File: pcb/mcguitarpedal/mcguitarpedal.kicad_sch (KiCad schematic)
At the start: 33 parts, among them SW1 LINE_LEVEL, U1 LM4562, U2 Teensy4.1, U3 Teensy4.0_AudioShield_REVD

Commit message: Schematic symbols
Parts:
- removed C1, C3, C4: 470n, symbol ltspice:cap
- removed C2: 570p, symbol ltspice:cap
- removed C5: 10µ, symbol ltspice:cap
- removed C6: 2.2n, symbol ltspice:cap
- removed C7: 4.7n, symbol ltspice:cap
- removed C7: 220n, symbol ltspice:cap
- removed COIL: 2.35, symbol ltspice:ind
- removed R, R10: 10k, symbol Device:R
- removed R1, R5, R6, R7, R8, R9: ${R_BIAS}, symbol Device:R
- removed R11: 4.7k, symbol Device:R
- removed R12: 2.2k, symbol Device:R
- removed R2, R4: ${R_BIAS_IN}, symbol Device:R
- removed R3: 250k, symbol Device:R
- removed R9: 1k, symbol Device:R
- removed RF: 10k, symbol Device:R_Variable
- removed RG: 500, symbol Device:R
- removed SW1: LINE_LEVEL, symbol Switch:SW_Slide_DPDT
- removed U1: LM4562, LM4562:lm4562, symbol Device:Opamp_Dual
- removed VIN: SINE(0 1 3k), symbol ltspice:voltage
- added J1: AudioJack3, Connector_Audio:Jack_6.35mm_Neutrik_NMJ6HFD2-AU_Horizontal, symbol Connector_Audio:AudioJack3
- added J2: Conn_01x05_Pin, Connector_PinHeader_2.54mm:PinHeader_1x05_P2.54mm_Vertical, symbol Connector:Conn_01x04_Pin
- added J3: BTN_MTX, symbol Connector_Generic:Conn_02x08_Row_Letter_Last
- added U4: 74LS148, symbol 74xx:74LS148
- added U5: HEF4094B, symbol 4xxx:HEF4094B
- added U6: LM7805_TO220, Package_TO_SOT_THT:TO-220-3_Vertical, symbol Regulator_Linear:LM7805_TO220
- U2: footprint (none) -> Package_DIP:DIP-48_W15.24mm_Socket_LongPads
- renumbered U3 to U1, V4 to V?, V1 to V?, V2 to V?
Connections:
- net 3.3V: now also U4.16 (VCC)
- net preamp/PREAMP_OUT: now reaches U1.35 (LINE_IN_L)
- net preamp/PREAMP_OUT: now also J2.5 (STAGE2_OUT)
- net at U2.24 (32_OUT1B): now also U4.14 (GS)
- net at U2.38 (16_A2_RX4_SCL1): now also U4.6 (S2)
- net at U2.40 (18_A4_SDA): now also U4.7 (S1)
- net at U2.41 (19_A5_SCL): now also U4.9 (S0)
- new net: J3.5a (Pin_5a), U4.1 (I4)
- new net: J3.1a (Pin_1a), U4.10 (IO)
- new net: J3.2a (Pin_2a), U4.11 (I1)
- new net: J3.3a (Pin_3a), U4.12 (I2)
- new net: J3.4a (Pin_4a), U4.13 (I3)
- new net: J3.6a (Pin_6a), U4.2 (I5)
- new net: J3.7a (Pin_7a), U4.3 (I6)
- new net: J3.8a (Pin_8a), U4.4 (I7)
- new net GND: J1.R, J1.S, J2.1 (GND), J3.1b (Pin_1b), J3.2b (Pin_2b), J3.3b (Pin_3b), J3.4b (Pin_4b), J3.5b (Pin_5b), J3.6b (Pin_6b), J3.7b (Pin_7b), J3.8b (Pin_8b), U4.15 (EO), U4.5 (EI), U4.8 (GND)
- new net preamp/PREAMP_IN: J1.T, J2.2 (PREAMP_IN)
- new net preamp/STAGE1_IN: J2.3 (STAGE1_IN)
- new net preamp/STAGE1_OUT: J2.4 (STAGE1_OUT)
- no-connect marks 0 -> 24
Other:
- added sheet preamp (preamp.kicad_sch)
- note removed: "* .lib LME49710.lib"
- note removed: ".ac dec 100 5 500k .save V(*?*) I(*?*)"
- note removed: ".noise V(PREAMP_OUT) VIN dec 100 2k 1Meg"
- note removed: ".param R=100k"
- note removed: ".param Rbin=1Meg"
- note removed: ".tran 0 15ms 0 100ns"
- note removed: "Instrument"
- note removed: "Line"
- moved on the sheet: U1, U2

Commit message: 4094 wiring
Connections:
- net 3.3V: now also U5.15 (OE), U5.16 (V_{DD})
- net GND: now also U5.8 (V_{SS})
- net at U2.22 (30_CRX3): now also U5.1 (STR)
- net at U2.35 (13_SCK_LED): now also U5.3 (CP)
- net at U2.36 (14_A0_TX3_SPDIF_OUT): now also U5.2 (D)
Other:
- moved on the sheet: J3, U4, U5

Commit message: ILI9488 schematic
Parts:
- removed V?: 5, symbol ltspice:voltage
- removed V?: 9, symbol ltspice:voltage
- added J4: OUT, Connector_Audio:Jack_6.35mm_Neutrik_NMJ6HCD2_Horizontal, symbol Connector_Audio:AudioJack3
- added J5: EXP, Connector_Audio:Jack_6.35mm_Neutrik_NMJ6HCD2_Horizontal, symbol Connector_Audio:AudioJack3
- added J6: ILI9488 Module, Connector_PinHeader_2.54mm:PinHeader_1x14_P2.54mm_Vertical, symbol Connector:Conn_01x14_Pin
- added J7: PWR_IN, symbol Connector:Barrel_Jack
- added U7: STDN-3A24-ADJ, Connector_PinSocket_2.54mm:PinSocket_1x04_P2.54mm_Vertical, symbol Regulator_Linear:LM7805_TO220
- J1: value AudioJack3 -> IN; footprint Connector_Audio:Jack_6.35mm_Neutrik_NMJ6HFD2-AU_Horizontal -> Connector_Audio:Jack_6.35mm_Neutrik_NMJ6HCD2_Horizontal
- J2: value Conn_01x05_Pin -> Conn_01x06_Pin; footprint Connector_PinHeader_2.54mm:PinHeader_1x05_P2.54mm_Vertical -> Connector_PinHeader_2.54mm:PinHeader_1x06_P2.54mm_Vertical
- J3: footprint (none) -> Connector_PinSocket_2.54mm:PinSocket_2x08_P2.54mm_Vertical
- U6: value LM7805_TO220 -> 7805 equivalent SMPS
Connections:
- net 3.3V: now also U1.40 (VOL_3.3V), U7.1 (VO)
- net 5V: now also U2.48 (VIN), U6.3 (VO), J6.1 (VCC), U7.3 (VI), U7.4 (EN)
- net 9V: now also U6.1 (VI), J7.1
- net GND: now also U1.38 (VOL_GND), U2.34 (GND), U2.47 (GND), U6.2 (GND), J6.2 (GND), J7.2, U7.2 (GND)
- net preamp/PREAMP_OUT: now also J2.6 (STAGE2_OUT), U1.34 (LINE_IN_R)
- net at U1.31 (LINE_OUT_L): now also J4.T
- net at U1.32 (LINE_OUT_GND): now also J4.R, J4.S
- net LED_STR: now reaches U2.22 (30_CRX3), U5.1 (STR)
- net 24_BTN_MTX_GS: now reaches U2.24 (32_OUT1B), U4.14 (GS)
- net 33_TFT_CS: now reaches U2.25 (33_MCLK2)
- net 33_TFT_CS: now also J6.3 (CS)
- net 34_TFT_RST: now reaches U2.26 (34_RX8)
- net 34_TFT_RST: now also J6.4 (RESET)
- net 35_TFT_DC/RS: now reaches U2.27 (35_TX8)
- net 35_TFT_DC/RS: now also J6.5 (DC/RS)
- net 36_TOUCH_CS: now reaches U2.28 (36_CS)
- net 36_TOUCH_CS: now also J6.11 (T_CS)
- net 37_TFT_T_IRQ: now reaches U2.29 (37_CS)
- net 37_TFT_T_IRQ: now also J6.14 (T_IRQ)
- net SCK: now reaches U2.35 (13_SCK_LED), U5.3 (CP)
- net LED_DATA: now reaches U2.36 (14_A0_TX3_SPDIF_OUT), U5.2 (D)
- new net 26_TFT_MOSI: J6.12 (T_DIN), J6.6 (SDI(MOSI))
- new net 27_TFT_SCLK: J6.10 (T_CLK), J6.7 (SCK)
- new net 39_TFT_MISO: J6.13 (T_DO), J6.9 (SDO(MISO))
- new net TFT_BACKLIGHT: J6.8 (LED)
- no-connect marks 24 -> 29
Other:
- moved on the sheet: J1, J3, U1, U2, U4, U5, U6

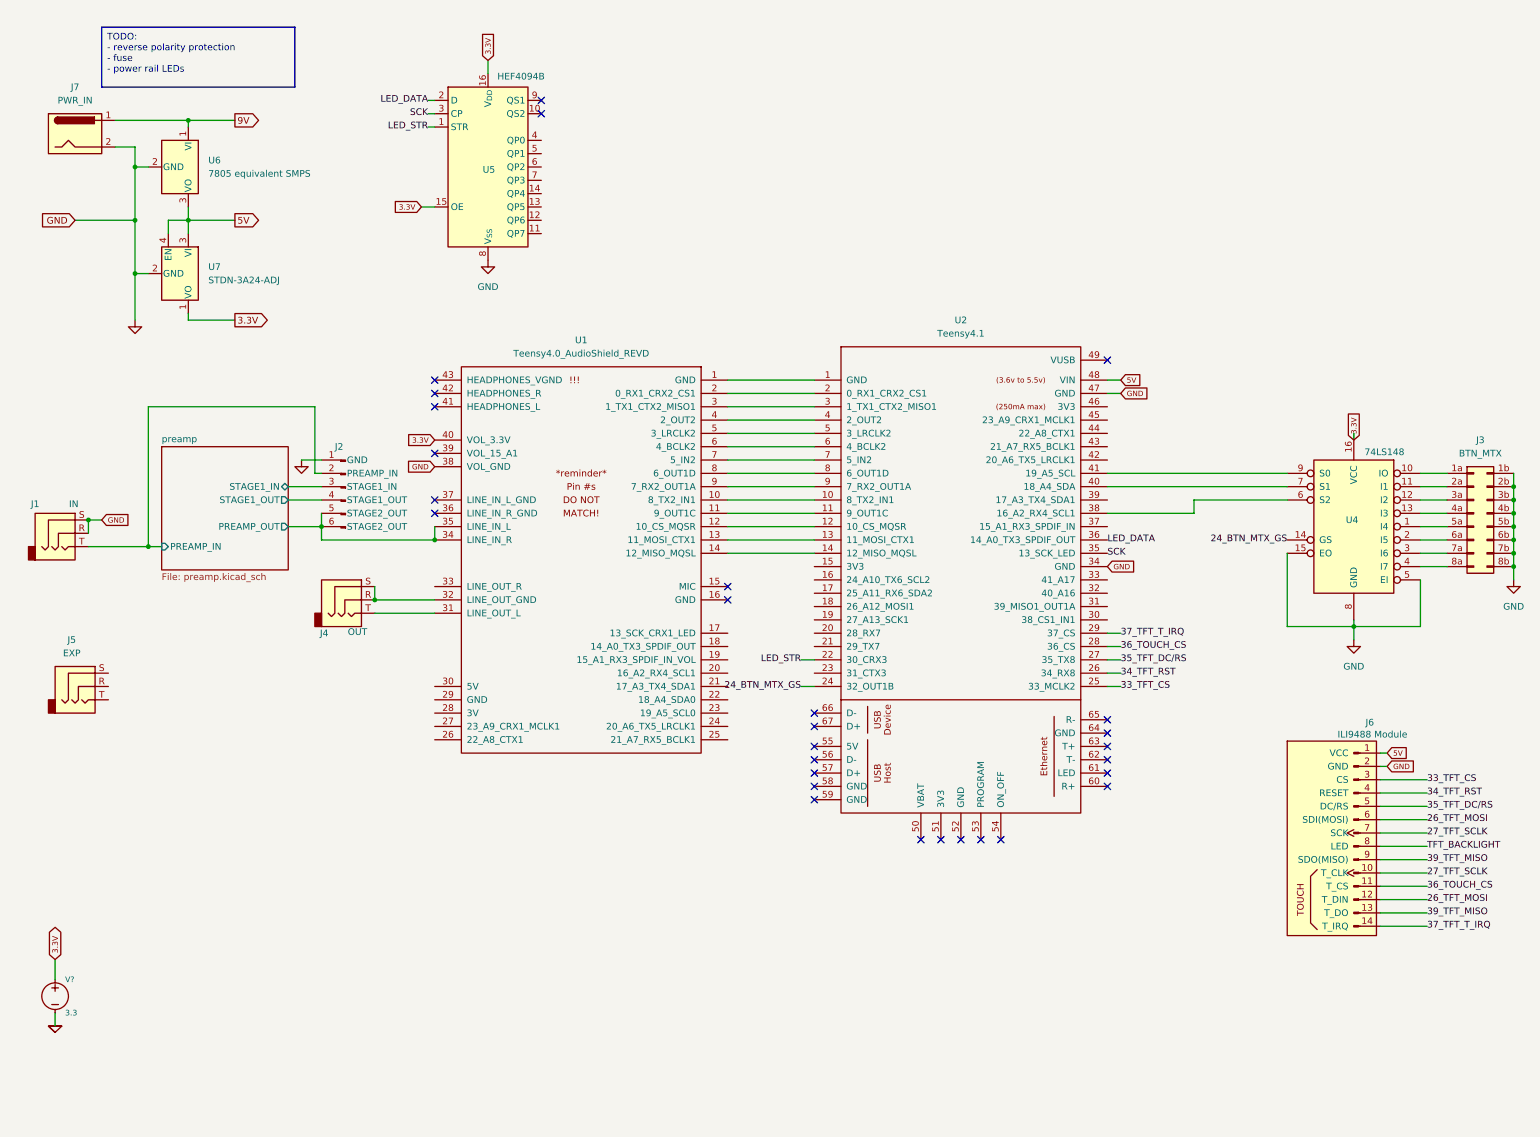
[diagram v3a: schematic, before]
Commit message: PCB physical layout
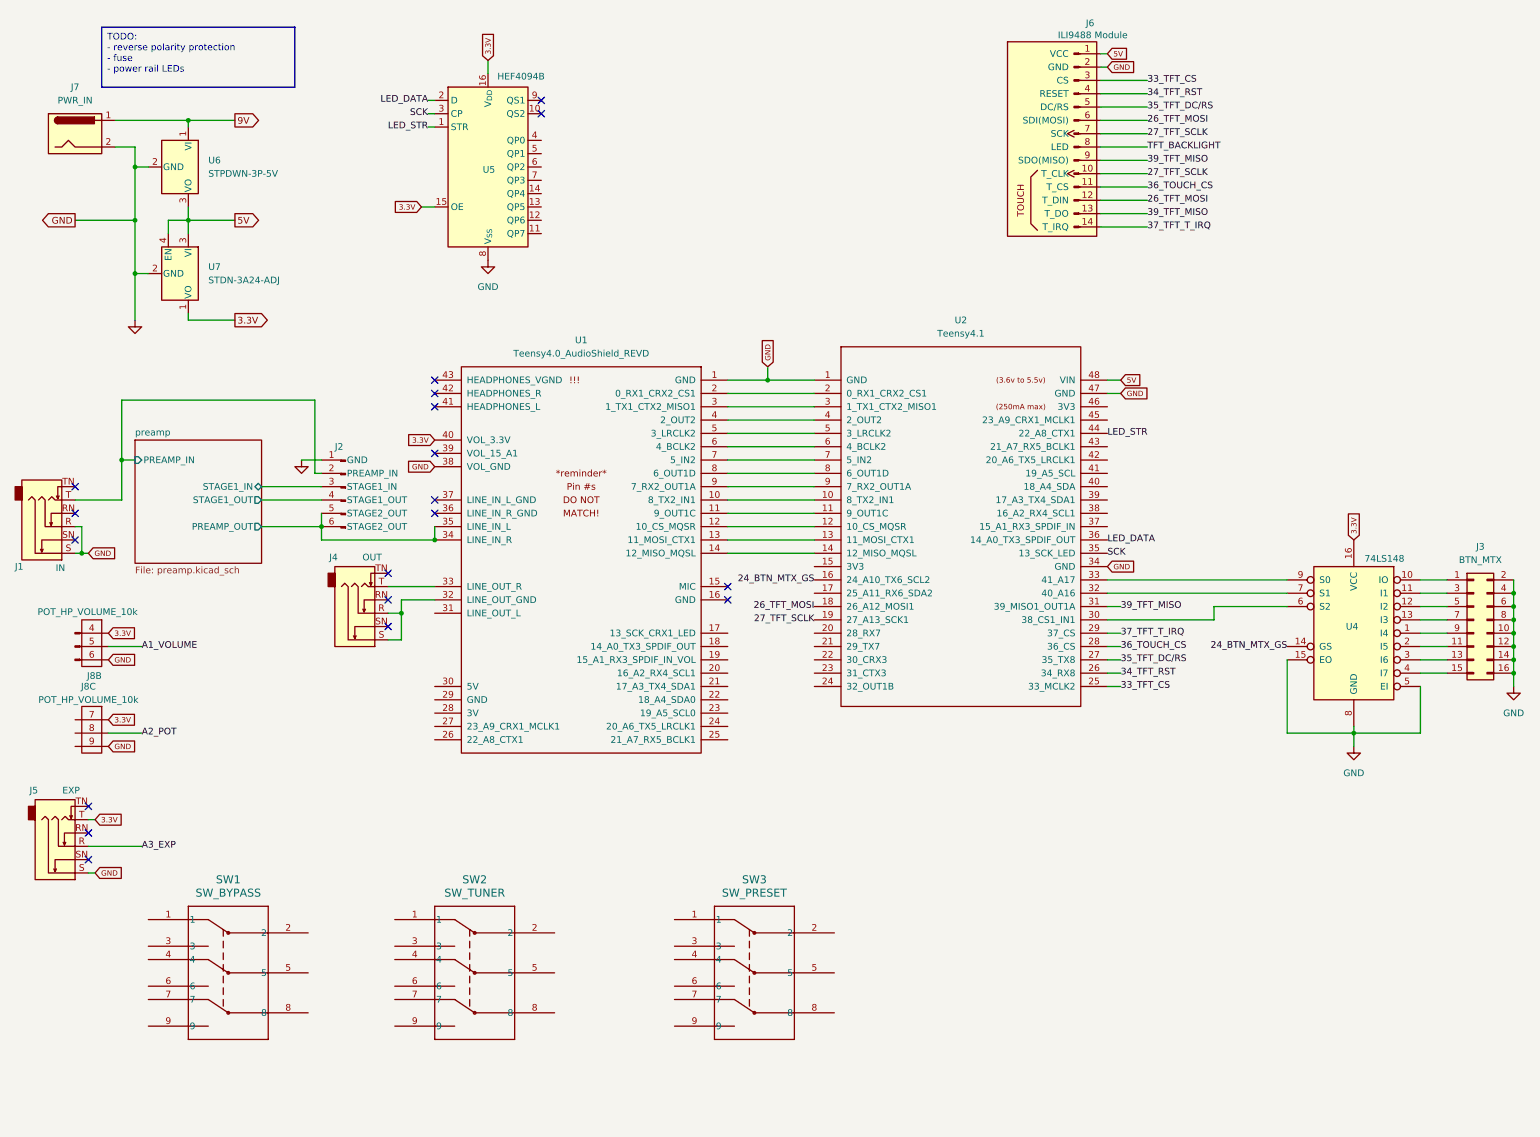
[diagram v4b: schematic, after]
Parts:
- removed V?: 3.3, symbol ltspice:voltage
- added J8: POT_HP_VOLUME_10k, Connector_PinHeader_2.54mm:PinHeader_1x09_P2.54mm_Vertical, symbol mcguitarpedal:3x2_Headers
- added SW1: SW_BYPASS, 01-690DB_3PDT_JCV, symbol 3PDT_FOOT_SWITCH:01-690DB-RH
- added SW2: SW_TUNER, 01-690DB_3PDT_JCV, symbol 3PDT_FOOT_SWITCH:01-690DB-RH
- added SW3: SW_PRESET, 01-690DB_3PDT_JCV, symbol 3PDT_FOOT_SWITCH:01-690DB-RH
- J1, J4, J5: symbol Connector_Audio:AudioJack3 -> Connector_Audio:AudioJack3_Switch
- J2: value Conn_01x06_Pin -> PREAMP_HEADERS
- J3: symbol Connector_Generic:Conn_02x08_Row_Letter_Last -> Connector_Generic:Conn_02x08_Odd_Even
- J6: footprint Connector_PinHeader_2.54mm:PinHeader_1x14_P2.54mm_Vertical -> ILI9488:ILI9488
- J7: footprint (none) -> Connector_PinHeader_2.54mm:PinHeader_2x02_P2.54mm_Vertical
- U1: footprint (none) -> teensy_audio_shield:4.0audioshield
- U2: symbol Teensy:Teensy4.1 -> Teensy (custom):Teensy4.1_(48_pins)
- U4: footprint (none) -> TI_FOOTPRINTS:DIP16_300_TEX
- U5: footprint (none) -> TI_FOOTPRINTS:N16
- U6: value 7805 equivalent SMPS -> STPDWN-3P-5V
- U7: symbol Regulator_Linear:LM7805_TO220 -> mcguitarpedal:STDN-3A24-ADJ
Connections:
- net 24_BTN_MTX_GS: now also U2.16 (24_A10_TX6_SCL2); no longer U2.24 (32_OUT1B)
- net 26_TFT_MOSI: now also U2.18 (26_A12_MOSI1)
- net 27_TFT_SCLK: now also U2.19 (27_A13_SCK1)
- net 3.3V: now also J5.T, J8.4 (Pin_4), J8.7 (Pin_7)
- net 39_TFT_MISO: now also U2.31 (39_MISO1_OUT1A)
- net GND: now also J3.10 (Pin_10), J3.12 (Pin_12), J3.14 (Pin_14), J3.16 (Pin_16), J3.2 (Pin_2), J3.4 (Pin_4), J3.6 (Pin_6), J3.8 (Pin_8), J5.S, U1.1 (GND), U2.1 (GND), J8.6 (Pin_6), J8.9 (Pin_9); no longer J3.1b (Pin_1b), J3.2b (Pin_2b), J3.3b (Pin_3b), J3.4b (Pin_4b), J3.5b (Pin_5b), J3.6b (Pin_6b), J3.7b (Pin_7b), J3.8b (Pin_8b)
- net LED_STR: now also U2.44 (22_A8_CTX1); no longer U2.22 (30_CRX3)
- net at U1.31 (LINE_OUT_L): no longer J4.T
- net at U1.33 (LINE_OUT_R): now also J4.T
- net A3_EXP: now reaches J5.R
- net at U2.30 (38_CS1_IN1): now also U4.6 (S2)
- net at U2.32 (40_A16): now also U4.7 (S1)
- net at U2.33 (41_A17): now also U4.9 (S0)
- net at U2.38 (16_A2_RX4_SCL1): no longer U4.6 (S2)
- net at U2.40 (18_A4_SDA): no longer U4.7 (S1)
- net at U2.41 (19_A5_SCL): no longer U4.9 (S0)
- net at U4.1 (I4): now also J3.9 (Pin_9); no longer J3.5a (Pin_5a)
- net at U4.10 (IO): now also J3.1 (Pin_1); no longer J3.1a (Pin_1a)
- net at U4.11 (I1): now also J3.3 (Pin_3); no longer J3.2a (Pin_2a)
- net at U4.12 (I2): now also J3.5 (Pin_5); no longer J3.3a (Pin_3a)
- net at U4.13 (I3): now also J3.7 (Pin_7); no longer J3.4a (Pin_4a)
- net at U4.2 (I5): now also J3.11 (Pin_11); no longer J3.6a (Pin_6a)
- net at U4.3 (I6): now also J3.13 (Pin_13); no longer J3.7a (Pin_7a)
- net at U4.4 (I7): now also J3.15 (Pin_15); no longer J3.8a (Pin_8a)
- new net A1_VOLUME: J8.5 (Pin_5)
- new net A2_POT: J8.8 (Pin_8)
- no-connect marks 29 -> 19
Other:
- moved on the sheet: J3, J6, U4

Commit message: Basic PCB routing
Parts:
- added D1: LED_BYPASS, LED_THT:LED_D5.0mm, symbol Device:LED
- added D2: LED_TUNER, LED_THT:LED_D5.0mm, symbol Device:LED
- added JP1: JP_SIGNAL_PREAMP, Connector_PinHeader_2.54mm:PinHeader_1x02_P2.54mm_Vertical, symbol Jumper:Jumper_2_Open
- added R13, R14: 150, Resistor_THT:R_Axial_DIN0207_L6.3mm_D2.5mm_P7.62mm_Horizontal, symbol Device:R
- J1, J4, J5: footprint Connector_Audio:Jack_6.35mm_Neutrik_NMJ6HCD2_Horizontal -> mcguitarpedal:Jack_6.35mm_Neutrik_NMJ6HCD2_Horizontal_3D_MODEL
- J3: footprint Connector_PinSocket_2.54mm:PinSocket_2x08_P2.54mm_Vertical -> Connector_PinHeader_2.54mm:PinHeader_2x08_P2.54mm_Vertical
- SW1, SW2, SW3: footprint 01-690DB_3PDT_JCV -> TI_FOOTPRINTS:01-690DB_3PDT_JCV_OVAL
- U1: footprint teensy_audio_shield:4.0audioshield -> teensy_audio_shield:4.0audioshield_reference
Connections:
- net preamp/PREAMP_IN is gone; now on net SIGNAL_IN: J1.T, J2.2 (PREAMP_IN)
- net 3.3V: now also SW1.7, SW2.7, R13.2, R14.2
- net A1_VOLUME: now also U2.37 (15_A1_RX3_SPDIF_IN)
- net A2_POT: now also U2.38 (16_A2_RX4_SCL1)
- net A3_EXP: now also U2.39 (17_A3_TX4_SDA1)
- net GND: now also J4.R, J4.S, SW1.6, SW1.9, SW2.9
- net 1_SW1: now reaches U1.2 (0_RX1_CRX2_CS1), U2.2 (0_RX1_CRX2_CS1)
- net 1_SW1: now also SW1.8, D1.1 (K)
- net at J4.T: now also SW1.2; no longer U1.33 (LINE_OUT_R)
- net 2_SW2: now reaches U1.4 (2_OUT2), U2.4 (2_OUT2)
- net 2_SW2: now also SW2.8, D2.1 (K)
- net at U4.1 (I4): now also J3.7 (Pin_7); no longer J3.9 (Pin_9)
- net at U4.10 (IO): now also J3.15 (Pin_15); no longer J3.1 (Pin_1)
- net at U4.11 (I1): now also J3.13 (Pin_13); no longer J3.3 (Pin_3)
- net at U4.12 (I2): now also J3.11 (Pin_11); no longer J3.5 (Pin_5)
- net at U4.13 (I3): now also J3.9 (Pin_9); no longer J3.7 (Pin_7)
- net at U4.2 (I5): now also J3.5 (Pin_5); no longer J3.11 (Pin_11)
- net at U4.3 (I6): now also J3.3 (Pin_3); no longer J3.13 (Pin_13)
- net at U4.4 (I7): now also J3.1 (Pin_1); no longer J3.15 (Pin_15)
- net SIGNAL_IN: now reaches SW1.1
- net SIGNAL_IN: now also SW1.4, JP1.1 (A)
- net LINE_OUT: now reaches SW1.3
- net LINE_OUT: now also U1.33 (LINE_OUT_R)
- net PREAMP_IN: now reaches SW1.5
- net PREAMP_IN: now also JP1.2 (B)
- new net: D2.2 (A), R14.1
- new net: D1.2 (A), R13.1
- now unconnected: U1.32 (LINE_OUT_GND)
- no-connect marks 19 -> 33
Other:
- moved on the sheet: J2, J4, J5, J8B, J8C, SW1, SW2, SW3

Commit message: Mostly routed board
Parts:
- added D3, D4, D5, D6, D7, D8: LED, LED_THT:LED_D3.0mm, symbol Device:LED_Small
- added JP2: JP_SCLK, Connector_PinHeader_2.54mm:PinHeader_1x02_P2.54mm_Vertical, symbol Jumper:Jumper_2_Open
- added JP3: JP_MISO, Connector_PinHeader_2.54mm:PinHeader_1x02_P2.54mm_Vertical, symbol Jumper:Jumper_2_Open
- added JP4: JP_MOSI, Connector_PinHeader_2.54mm:PinHeader_1x02_P2.54mm_Vertical, symbol Jumper:Jumper_2_Open
- added R15, R16, R17: 50, Resistor_SMD:R_1206_3216Metric_Pad1.30x1.75mm_HandSolder, symbol Device:R
- added R18, R19, R20, R21, R22, R23: 150, Resistor_SMD:R_1206_3216Metric_Pad1.30x1.75mm_HandSolder, symbol Device:R_Small
- D1, D2: symbol Device:LED -> Device:LED_Small
- J7: footprint Connector_PinHeader_2.54mm:PinHeader_2x02_P2.54mm_Vertical -> Connector_BarrelJack:BarrelJack_Kycon_KLDX-0202-xC_Horizontal
- R13, R14: footprint Resistor_THT:R_Axial_DIN0207_L6.3mm_D2.5mm_P7.62mm_Horizontal -> Resistor_SMD:R_1206_3216Metric_Pad1.30x1.75mm_HandSolder; symbol Device:R -> Device:R_Small
- U2: footprint Package_DIP:DIP-48_W15.24mm_Socket_LongPads -> mcguitarpedal:PinHeader_2x24_P2.54mm_W15.24_Vertical
- U4: value 74LS148 -> 74HC148
- U5: value HEF4094B -> 74HC4094
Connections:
- net 26_TFT_MOSI: now also JP4.2 (B), R15.2; no longer J6.12 (T_DIN), J6.6 (SDI(MOSI))
- net 27_TFT_SCLK: now also JP2.2 (B), R16.2; no longer J6.10 (T_CLK), J6.7 (SCK)
- net 3.3V: now also D3.2 (A), D4.2 (A), D5.2 (A), D6.2 (A), D7.2 (A), D8.2 (A)
- net 39_TFT_MISO: now also JP3.2 (B), R17.2; no longer J6.13 (T_DO), J6.9 (SDO(MISO))
- net at U5.13 (QP5): now also R23.1
- net at U5.14 (QP4): now also R22.1
- net at U5.4 (QP0): now also R18.1
- net at U5.5 (QP1): now also R19.1
- net at U5.6 (QP2): now also R20.1
- net at U5.7 (QP3): now also R21.1
- new net: J6.12 (T_DIN), J6.6 (SDI(MOSI)), JP4.1 (A), R15.1
- new net: J6.10 (T_CLK), J6.7 (SCK), JP2.1 (A), R16.1
- new net: D6.1 (K), R21.2
- new net: J6.13 (T_DO), J6.9 (SDO(MISO)), JP3.1 (A), R17.1
- new net: D7.1 (K), R22.2
- new net: D4.1 (K), R19.2
- new net: D8.1 (K), R23.2
- new net: D5.1 (K), R20.2
- new net: D3.1 (K), R18.2
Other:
- note added: "D3-D8 LED"
- note added: "R18-23 150"
- moved on the sheet: D1, D2, J6
